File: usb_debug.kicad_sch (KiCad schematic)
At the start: 4 parts, among them U1 MIMXRT1052CVJ5B

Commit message: finished v1
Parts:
- added C52: 100nF, Capacitor_SMD:C_0402_1005Metric, symbol Device:C
- added C53, C54: 1uF, Capacitor_SMD:C_0402_1005Metric, symbol Device:C_Small
- added F1: ASMD1206-150, Fuse:Fuse_1206_3216Metric, symbol Device:Polyfuse
- added IC3: ADP3338AKCZ-5-REEL, SOT230P700X180-4N, symbol SamacSys_Parts:ADP3338AKCZ-5-REEL
- added J5: USB_C_Receptacle_USB2.0, Connector_USB:USB_C_Receptacle_HRO_TYPE-C-31-M-12, symbol Connector:USB_C_Receptacle_USB2.0
- added L2: 60R@100MHz, Inductor_SMD:L_1206_3216Metric, symbol Unified-Daughterboard-rescue:L_Core_Ferrite-Device
- added R7, R8: 5.1k, Resistor_SMD:R_0402_1005Metric_Pad0.72x0.64mm_HandSolder, symbol Device:R_US
- added U7: PRTR5V0U2X, Package_TO_SOT_SMD:SOT-143, symbol Power_Protection:PRTR5V0U2X
- added U8: XC6206P332PR-G, Package_TO_SOT_SMD:SOT-23, symbol kicad-keyboard-parts:XC6206PxxxMR-Regulator_Linear
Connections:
- net GND: now also C52.2, C53.1, C54.1, IC3.1 (GND), J5.A1 (GND), J5.A12 (GND), J5.B1 (GND), J5.B12 (GND), J5.S1 (SHIELD), L2.1, L2.2, R7.1, R8.1, U7.1 (GND), U8.1 (GND)
- net USB_OTG1_DN: now also J5.A7 (D-), J5.B7 (D-)
- net USB_OTG1_DP: now also J5.A6 (D+), J5.B6 (D+)
- new net: J5.A5 (CC1), R7.2
- new net: J5.B5 (CC2), R8.2
- new net +3.3V: C54.2, U8.2 (VO)
- new net +5V: C53.2, IC3.2 (OUT_1), IC3.4 (OUT_2), U8.3 (VI)
- new net D_N: U7.2 (I/O1)
- new net D_P: U7.3 (I/O2)
- new net VBUS: F1.1, J5.A4 (VBUS), J5.A9 (VBUS), J5.B4 (VBUS), J5.B9 (VBUS)
- new net VBUS_fuse: C52.1, F1.2, IC3.3 (IN), U7.4 (VCC)
- no-connect marks 4 -> 6
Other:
- note added: "UFP pull down"
- company: (none) -> Northeastern University
- title: (none) -> RT1050 DevBoard for Project Horizon
- moved on the sheet: C32, C33, C34, U1F

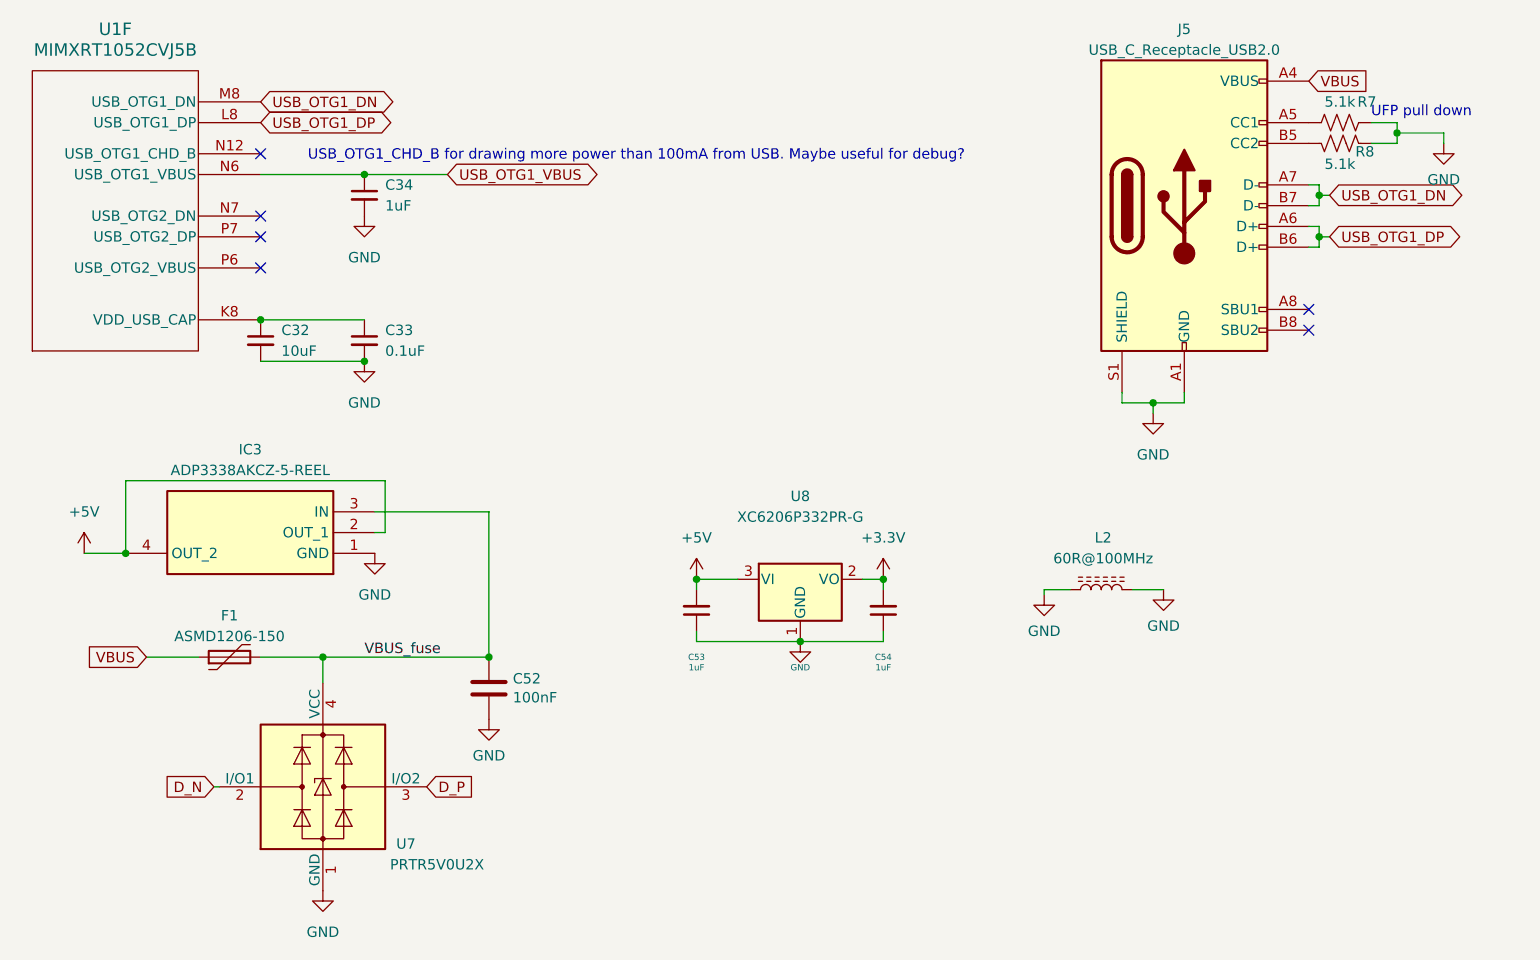
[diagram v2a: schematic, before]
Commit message: added load switches
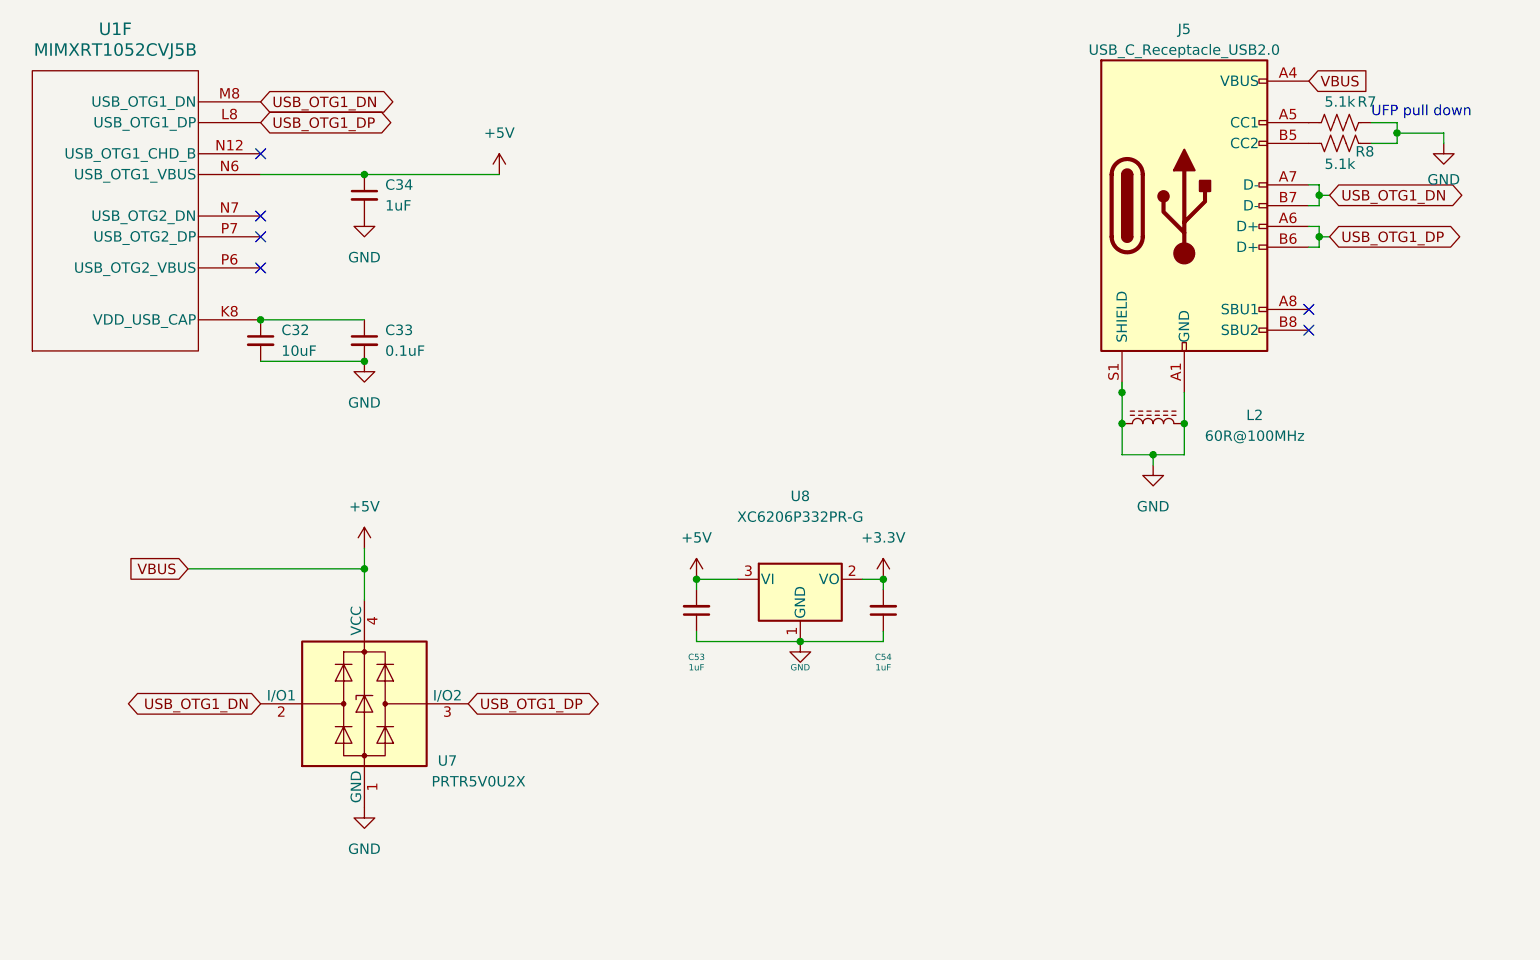
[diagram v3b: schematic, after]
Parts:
- removed C52: 100nF, Capacitor_SMD:C_0402_1005Metric, symbol Device:C
- removed F1: ASMD1206-150, Fuse:Fuse_1206_3216Metric, symbol Device:Polyfuse
- removed IC3: ADP3338AKCZ-5-REEL, SOT230P700X180-4N, symbol SamacSys_Parts:ADP3338AKCZ-5-REEL
- C32, C33, C34: footprint (none) -> Capacitor_SMD:C_0402_1005Metric
- R7, R8: footprint Resistor_SMD:R_0402_1005Metric_Pad0.72x0.64mm_HandSolder -> Resistor_SMD:R_0402_1005Metric
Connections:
- net D_N is gone; now on net USB_OTG1_DN: U7.2 (I/O1)
- net D_P is gone; now on net USB_OTG1_DP: U7.3 (I/O2)
- net USB_OTG1_VBUS is gone; now on net +5V: C34.1, U1.N6 (USB_OTG1_VBUS)
- net VBUS is gone; now on net +5V: J5.A4 (VBUS), J5.A9 (VBUS), J5.B4 (VBUS), J5.B9 (VBUS)
- net VBUS_fuse is gone; now on net +5V: U7.4 (VCC)
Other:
- note removed: "USB_OTG1_CHD_B for drawing more power than 100mA from USB. Maybe useful for debug?"
- moved on the sheet: U7

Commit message: save before sdram redesign
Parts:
- added R13, R14, R15: 1k, Resistor_SMD:R_0402_1005Metric, symbol Device:R_Small_US
- added R16, R17, R18: 10k, Resistor_SMD:R_0402_1005Metric, symbol Device:R_Small_US
- added SW1: SW_DIP_x02, Button_Switch_SMD:SW_DIP_SPSTx02_Slide_6.7x6.64mm_W6.73mm_P2.54mm_LowProfile_JPin, symbol Switch:SW_DIP_x02
- C32, C33, C34, C53, C54: footprint Capacitor_SMD:C_0402_1005Metric -> Capacitor_SMD:C_0201_0603Metric
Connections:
- net +3.3V: now also R13.1, R14.1, R15.1
- net GND: now also R16.1, R17.1, R18.2
- new net: R15.2, SW1.3
- new net: R14.2, SW1.4
- new net GPIO_AD_B0_04: R18.1, SW1.2
- new net GPIO_AD_B0_05: R17.2, SW1.1
- new net GPIO_B0_13: R13.2, R16.2
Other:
- note removed: "UFP pull down"
- moved on the sheet: J5, L2, R7, R8
